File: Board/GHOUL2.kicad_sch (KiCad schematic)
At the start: 32 parts, among them M1 Motor_Servo, U1 Teensy4.1, U2 DS18S20, U3 CAM-M8Q-0, U4 TPS62133, U5 MS5607-02BA

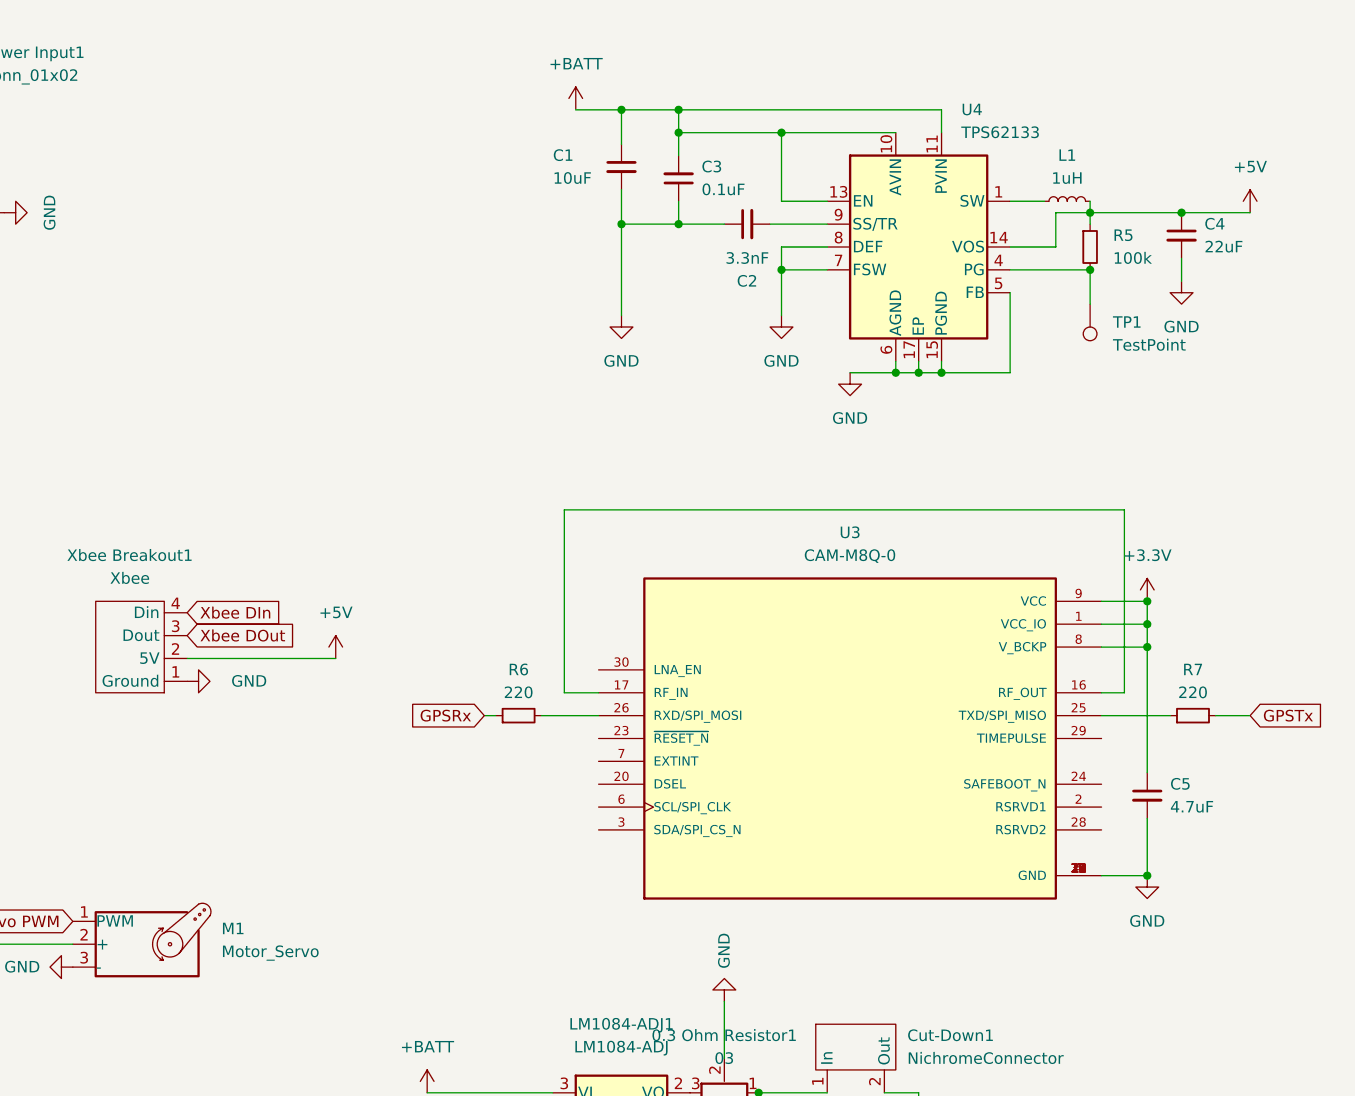
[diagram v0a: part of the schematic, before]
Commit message: added SAM and changed PCB
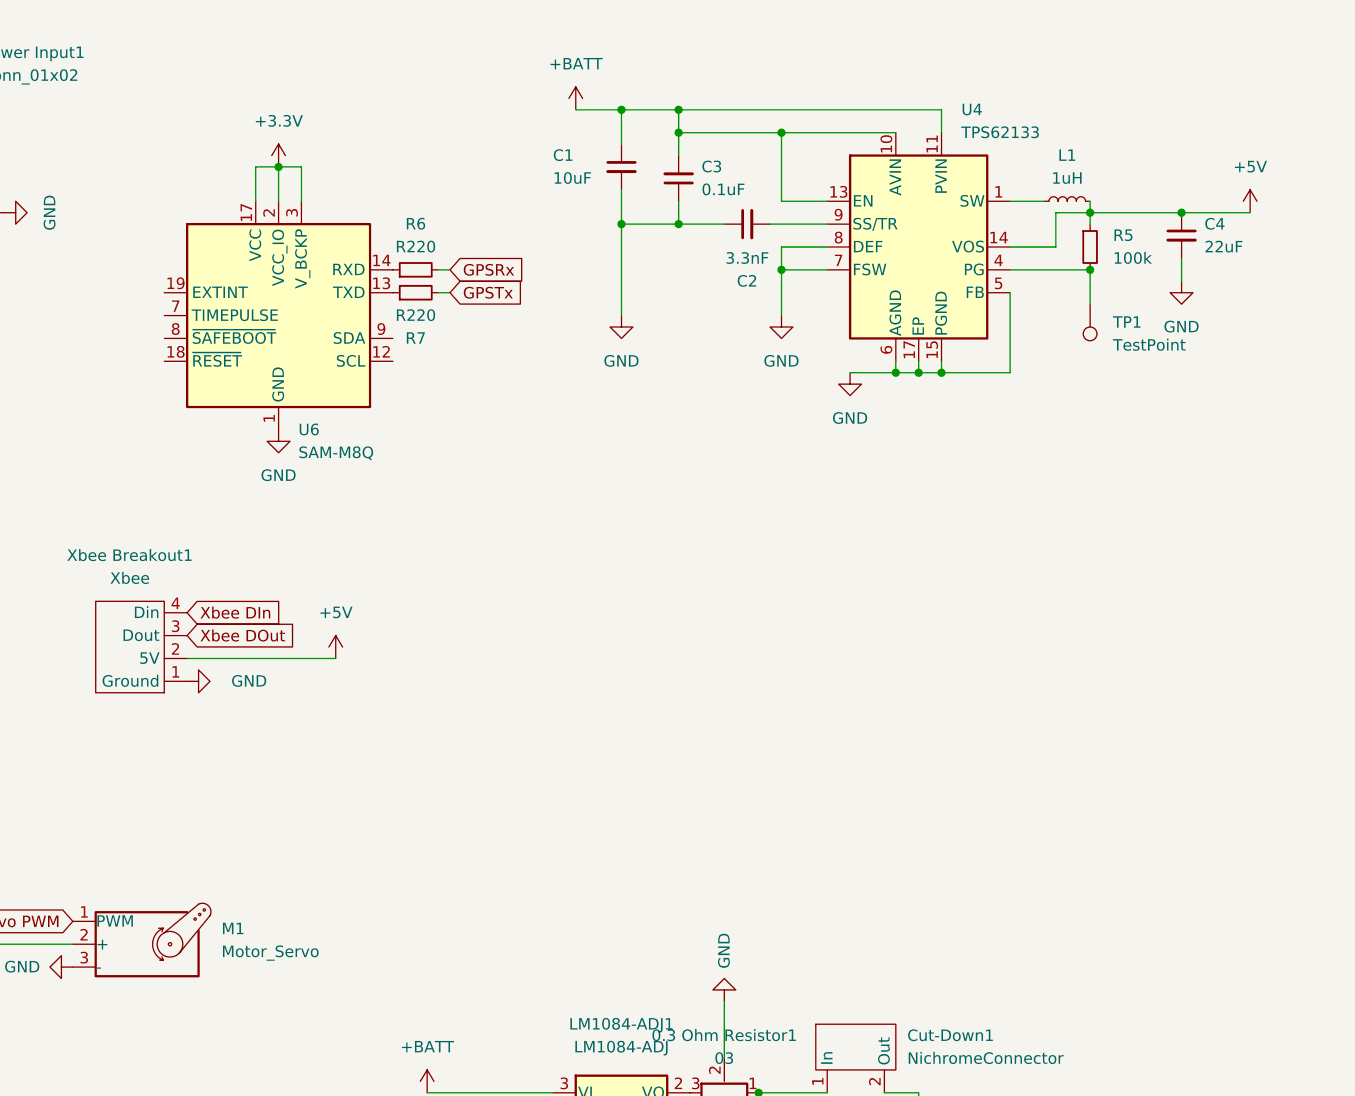
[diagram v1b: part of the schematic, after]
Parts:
- removed C5: 4.7uF, Capacitor_SMD:C_0603_1608Metric_Pad1.08x0.95mm_HandSolder, symbol Device:C_Small
- removed U3: CAM-M8Q-0, CAM-M8Q-0:LCC100P960X1400X210-31N, symbol CAM-M8Q-0:CAM-M8Q-0
- added U6: SAM-M8Q, RF_GPS:ublox_SAM-M8Q, symbol RF_GPS:SAM-M8Q
- R6, R7: value 220 -> R220; footprint Resistor_SMD:R_0603_1608Metric_Pad0.98x0.95mm_HandSolder -> Resistor_SMD:R_0201_0603Metric_Pad0.64x0.40mm_HandSolder
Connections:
- net +3.3V: now also U6.17 (VCC), U6.2 (VCC_IO), U6.3 (V_BCKP)
- net GND: now also U6.1 (GND), U6.10 (GND), U6.11 (GND), U6.15 (GND), U6.16 (GND), U6.20 (GND), U6.4 (GND), U6.5 (GND), U6.6 (GND)
- net GPSRx: now also R6.2; no longer R6.1
- net at R7.1: now also U6.13 (TXD)
- new net: R6.1, U6.14 (RXD)

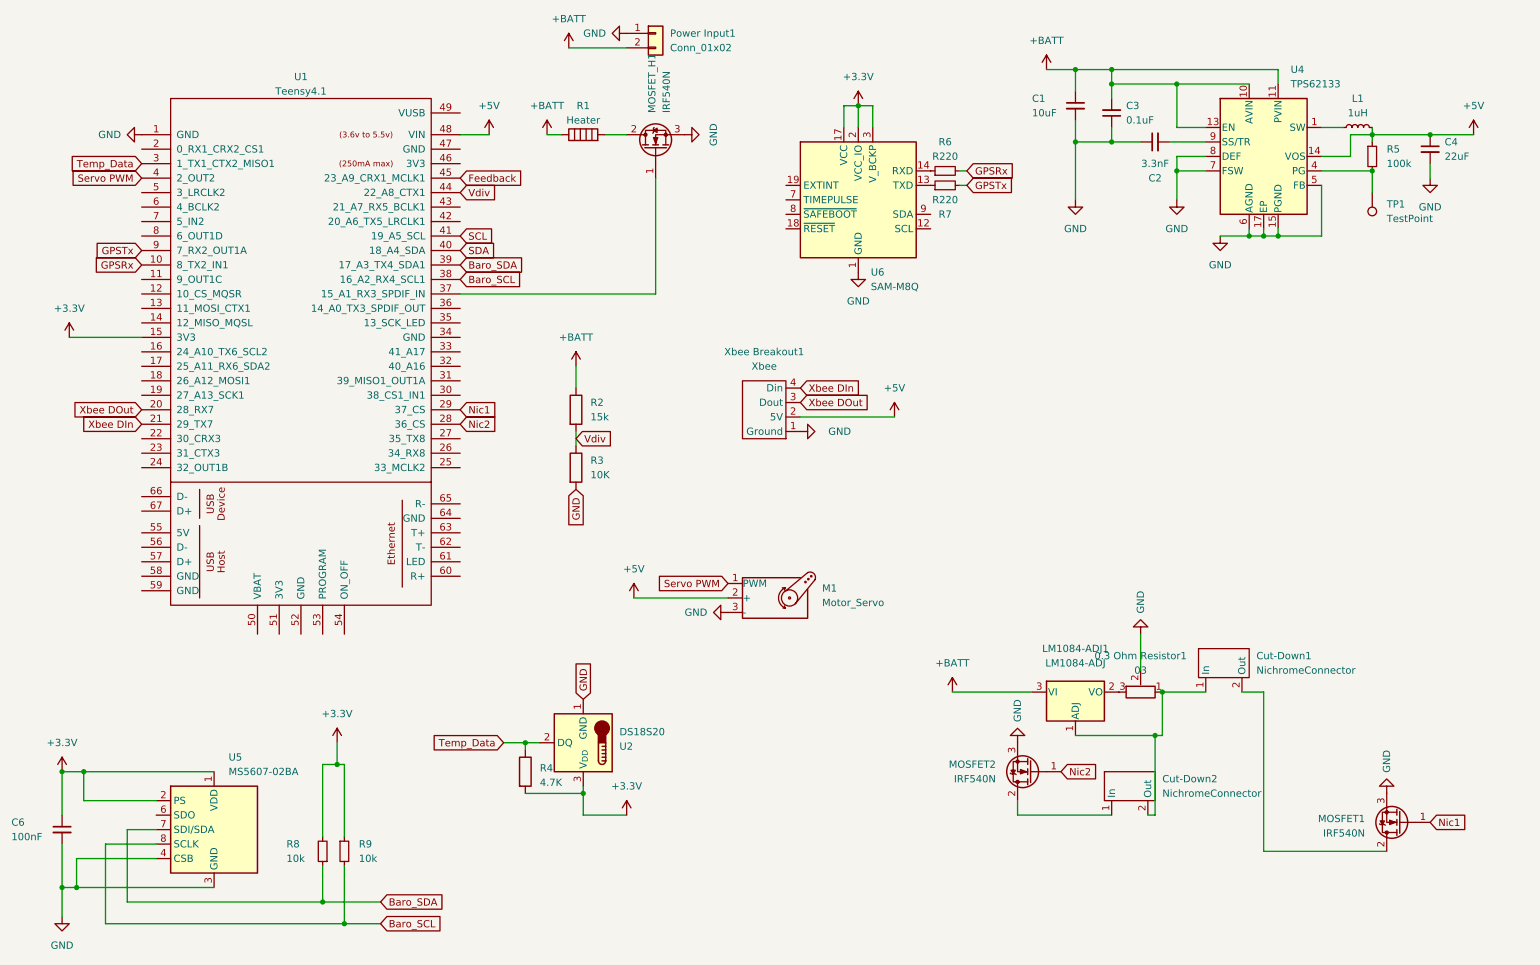
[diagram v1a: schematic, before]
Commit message: added teensy rtc
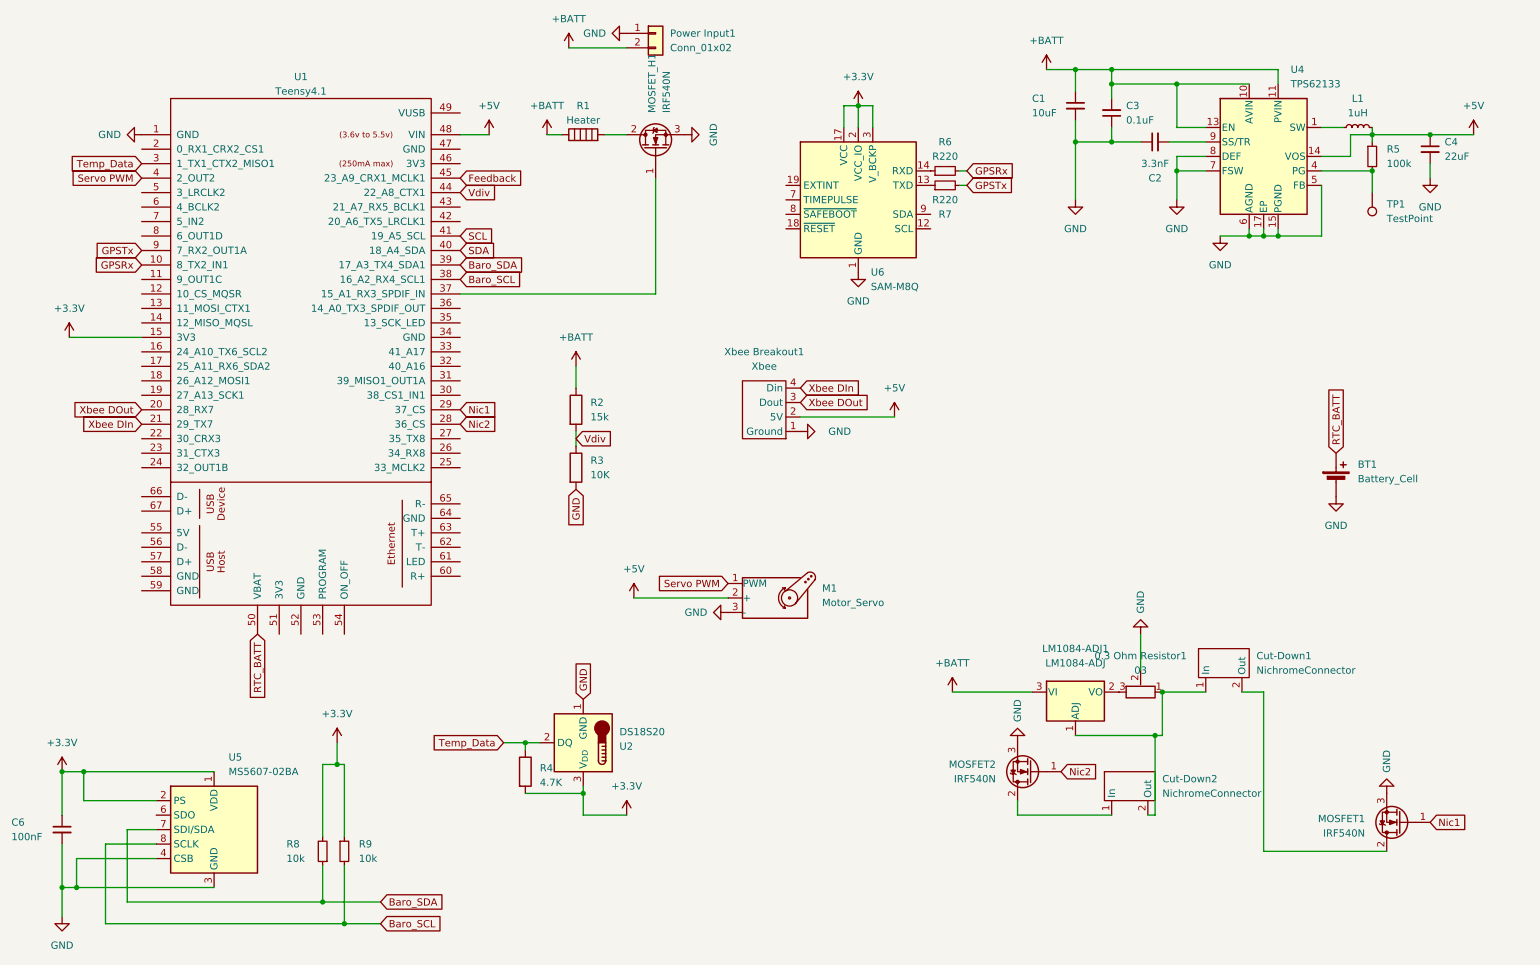
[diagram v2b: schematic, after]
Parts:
- added BT1: Battery_Cell, Battery:BatteryHolder_Keystone_3000_1x12mm, symbol Device:Battery_Cell
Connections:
- net GND: now also BT1.2 (-)
- net RTC_BATT: now reaches U1.50 (VBAT)
- net RTC_BATT: now also BT1.1 (+)
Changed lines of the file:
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@@
+    )
+  )
+  (global_label "RTC_BATT" (shape input) (at 60.96 124.46 270) (fields_autoplaced)
+    (effects (font (size 1.27 1.27)) (justify right))
+    (property "Intersheetrefs" "${INTERSHEET_REFS}" (at 60.96 136.2142 90)
+      (effects (font (size 1.27 1.27)) (justify right) hide)
+    )
+  )
+  (global_label "RTC_BATT" (shape input) (at 250.19 92.71 90) (fields_autoplaced)
+    (effects (font (size 1.27 1.27)) (justify left))
+    (property "Intersheetrefs" "${INTERSHEET_REFS}" (at 250.19 80.9558 90)
+      (effects (font (size 1.27 1.27)) (justify left) hide)
     )
   )
@@
         (path "/a2e390a1-3d20-4e85-b6dd-da84eefdc6ca"
           (reference "C4") (unit 1)
+        )
+      )
+    )
+  )
+  (symbol (lib_name "GND_7") (lib_id "power:GND") (at 250.19 100.33 0) (unit 1)
+    (in_bom yes) (on_board yes) (dnp no) (fields_autoplaced)
+    (property "Reference" "#PWR09" (at 250.19 106.68 0)
+      (effects (font (size 1.27 1.27)) hide)
+    )
+    (property "Value" "GND" (at 250.19 105.41 0)
+      (effects (font (size 1.27 1.27)))
+    )
+    (property "Footprint" "" (at 250.19 100.33 0)
+      (effects (font (size 1.27 1.27)) hide)
+    )
+    (property "Datasheet" "" (at 250.19 100.33 0)
+      (effects (font (size 1.27 1.27)) hide)
+    )
+    (pin "1")
+    (instances
+      (project "GHOUL2"
+        (path "/a2e390a1-3d20-4e85-b6dd-da84eefdc6ca"
+          (reference "#PWR09") (unit 1)
         )
       )
@@
         )
       )
+    )
+  )
+  (symbol (lib_id "Device:Battery_Cell") (at 250.19 97.79 0) (unit 1)
+    (in_bom yes) (on_board yes) (dnp no) (fields_autoplaced)
+    (property "Reference" "BT1" (at 254 94.6785 0)
+      (effects (font (size 1.27 1.27)) (justify left))
+    )
+    (property "Value" "Battery_Cell" (at 254 97.2185 0)
+      (effects (font (size 1.27 1.27)) (justify left))
+    )
+    (property "Footprint" "Battery:BatteryHolder_Keystone_3000_1x12mm" (at 250.19 96.266 90)
+      (effects (font (size 1.27 1.27)) hide)
+    )
+    (property "Datasheet" "~" (at 250.19 96.266 90)
+      (effects (font (size 1.27 1.27)) hide)
+    )
+    (pin "1")
+    (pin "2")
+    (instances
+      (project "GHOUL2"
+        (path "/a2e390a1-3d20-4e85-b6dd-da84eefdc6ca"
+          (reference "BT1") (unit 1)
+        )
+      )
